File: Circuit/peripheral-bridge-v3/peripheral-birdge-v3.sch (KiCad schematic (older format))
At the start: 76 parts, among them CON1 Conn-Edge-PCIE-x1, J1 To DVL, J2 Pressure Sensor, J3 Solenoid, J4 USB_OTG, J5 DSP_Reset, P1 Solenoid Power, Q1 BSS138, U1 FT2232H, U2 93LC56BT-I/OT, U3 ADM3251E, U4 ADC101S021, U5 ACPL-247-500E, U6 ACPL-247-500E, U7 LM1117-33, Y1 12MHz

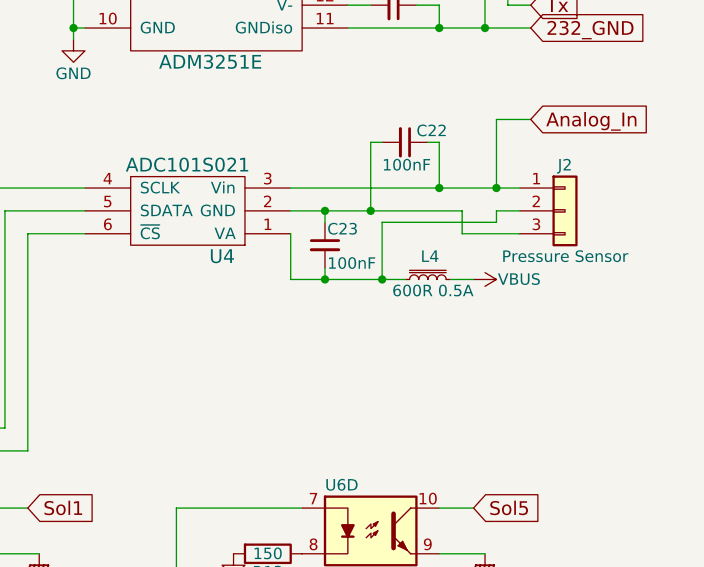
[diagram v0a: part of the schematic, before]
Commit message: add gnd in pressure sensor line(ComBridgeV3) and add L C in pressure sensor line(BackPlane)
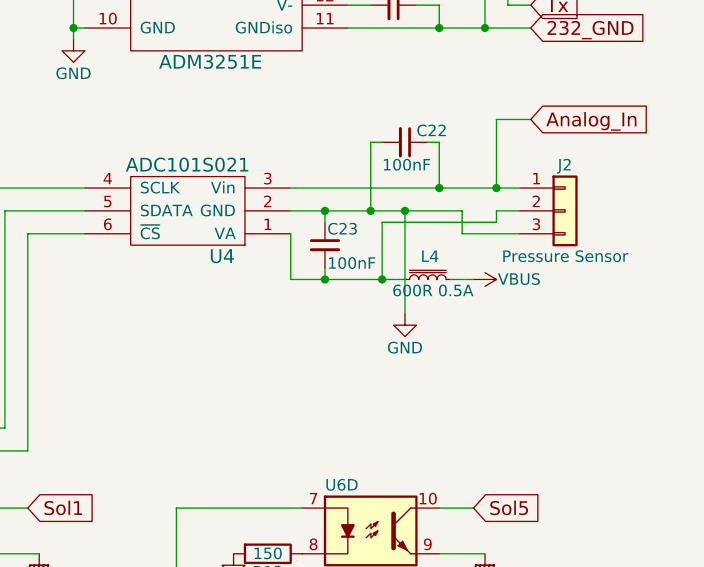
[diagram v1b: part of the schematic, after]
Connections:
- net GND: now also C22.2, C23.1, J2.3 (Pin_3), U4.2 (GND)
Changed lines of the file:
@@
 Wire Wire Line
 	10450 5950 10450 5900
+Wire Wire Line
+	10050 2950 10050 3400
+Connection ~ 10050 2950
+$Comp
+L GND #PWR?
+U 1 1 5A691AB4
+P 10050 3400
+F 0 "#PWR?" H 10050 3150 50  0001 C CNN
+F 1 "GND" H 10050 3250 50  0000 C CNN
+F 2 "" H 10050 3400 50  0001 C CNN
+F 3 "" H 10050 3400 50  0001 C CNN
+	1    10050 3400
+	1    0    0    -1
+$EndComp
 $EndSCHEMATC
